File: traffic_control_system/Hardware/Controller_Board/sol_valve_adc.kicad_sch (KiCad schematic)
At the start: 45 parts, among them U21 TL084, U22 TL081, U23 APX321SEG

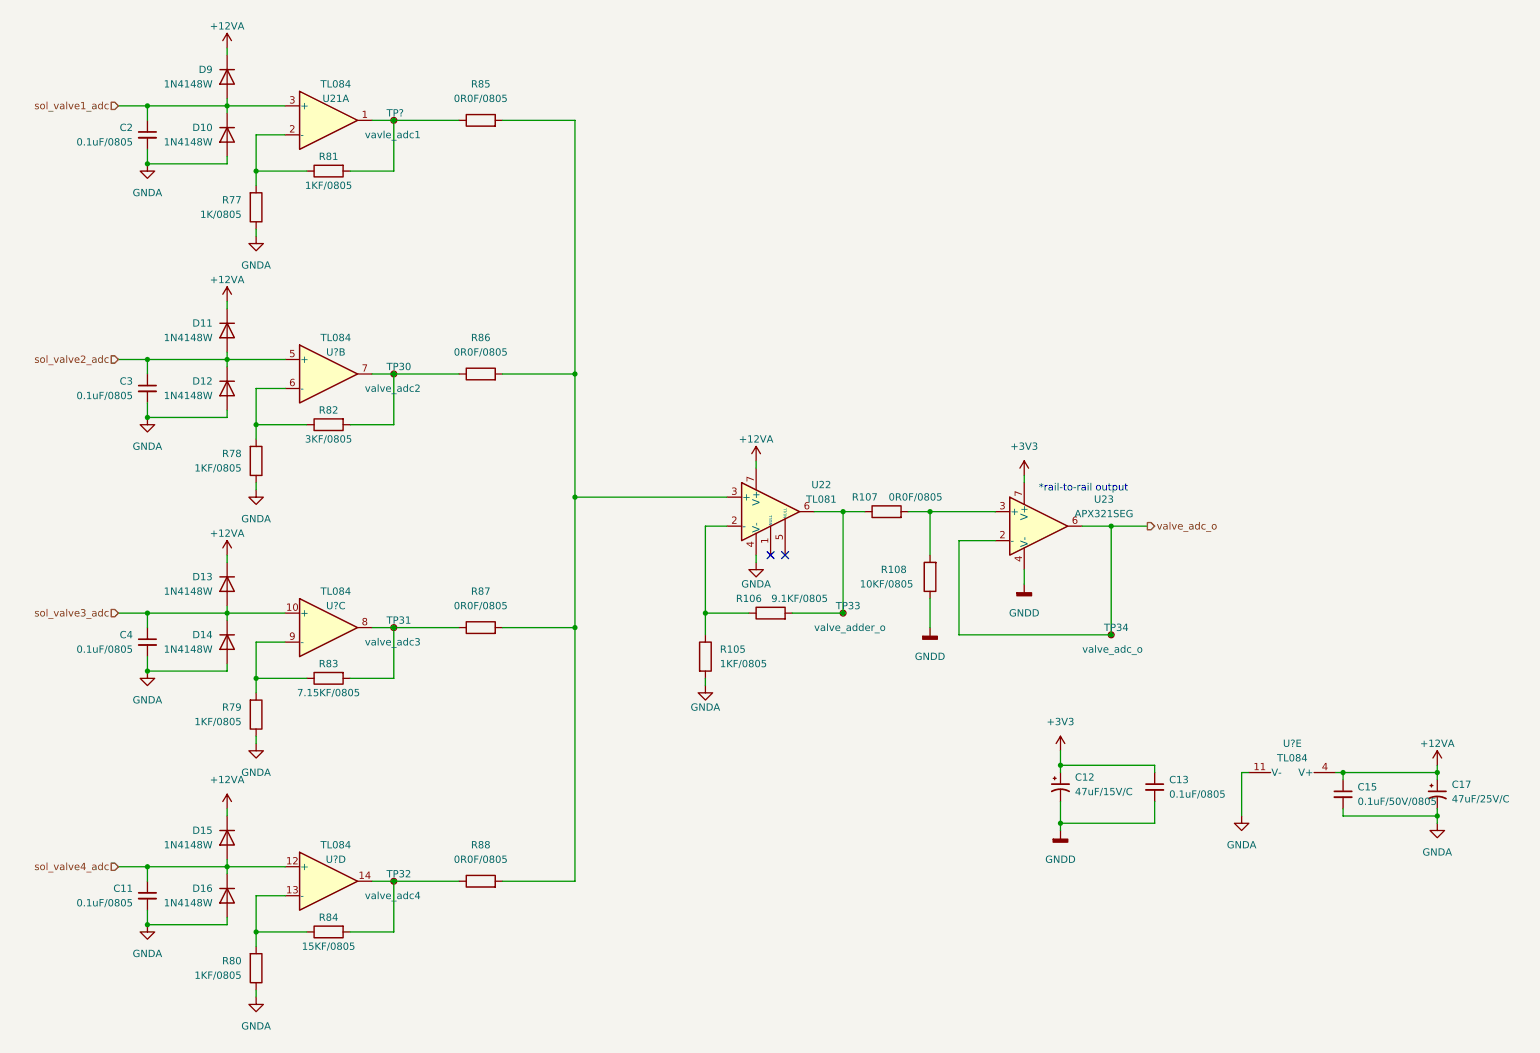
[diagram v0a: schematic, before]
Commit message: issue : 깃 커밋 히스토리 정리를 위한 원본 저장소의 브랜치 분리 작업[TRAFFIC-CONTROL6]
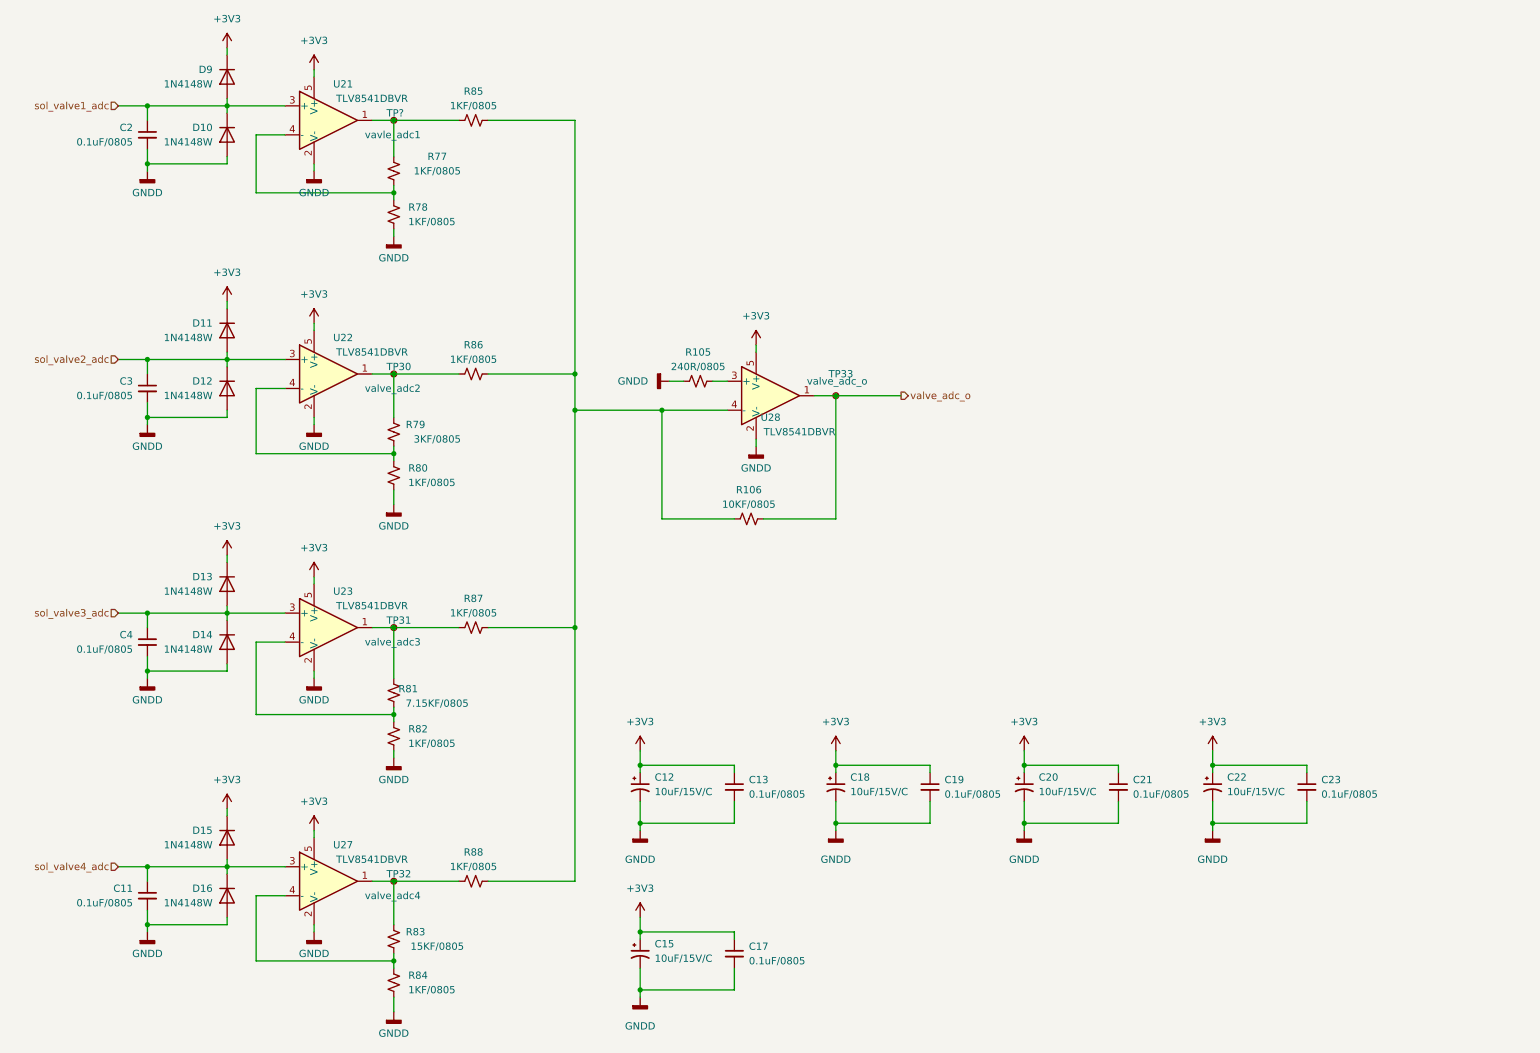
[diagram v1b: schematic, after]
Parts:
- removed C15: 0.1uF/50V/0805, symbol Device:C_Small
- removed C17: 47uF/25V/C, symbol Device:C_Polarized_Small_US
- removed R105, R77, R78, R79, R80, R81: 1KF/0805, symbol Device:R
- removed R106: 9.1KF/0805, symbol Device:R
- removed R107, R86, R87, R88: 0R0F/0805, symbol Device:R
- removed R108: 10KF/0805, symbol Device:R
- removed R82: 3KF/0805, symbol Device:R
- removed R83: 7.15KF/0805, symbol Device:R
- removed R84: 15KF/0805, symbol Device:R
- removed R85: R, symbol Device:R
- removed TP34: valve_adc_o, symbol Connector:TestPoint_Small
- removed U21, U? (x4): TL084, symbol Amplifier_Operational:TL084
- removed U22: TL081, symbol Amplifier_Operational:TL081
- removed U23: APX321SEG, Package_SO:SOIC-8_3.9x4.9mm_P1.27mm, symbol Amplifier_Operational:OPA196xD
- added C15, C18, C20, C22: 10uF/15V/C, symbol Device:C_Polarized_Small_US
- added C17, C19, C21, C23: 0.1uF/0805, symbol Device:C_Small
- added R105: 240R/0805, symbol Device:R_Small_US
- added R106: 10KF/0805, symbol Device:R_Small_US
- added R77, R78, R80, R82, R84, R85, R86, R87, R88: 1KF/0805, symbol Device:R_Small_US
- added R79: 3KF/0805, symbol Device:R_Small_US
- added R81: 7.15KF/0805, symbol Device:R_Small_US
- added R83: 15KF/0805, symbol Device:R_Small_US
- added U21, U22, U23, U27, U28: TLV8541DBVR, Package_TO_SOT_SMD:SOT-23-5, symbol Amplifier_Operational:TLV2371DBV
- C12: value 47uF/15V/C -> 10uF/15V/C
- TP33: value valve_adder_o -> valve_adc_o
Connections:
- net +12VA is gone; now on net +3V3: D11.1 (K), D13.1 (K), D15.1 (K), D9.1 (K)
- net GNDA is gone; now on net GNDD: C11.2, C2.2, C3.2, C4.2, D10.2 (A), D12.2 (A), D14.2 (A), D16.2 (A)
- net +3V3: now also C15.1, C17.1, C18.1, C19.1, C20.1, C21.1, C22.1, C23.1, U21.5 (V+), U22.5 (V+), U23.5 (V+), U27.5 (V+), U28.5 (V+)
- net GNDD: now also C15.2, C17.2, C18.2, C19.2, C20.2, C21.2, C22.2, C23.2, R105.2, R78.1, R80.1, R82.1, R84.1, U21.2 (V-), U22.2 (V-), U23.2 (V-), U27.2 (V-), U28.2 (V-)
- net sol_valve1_adc: now also U21.3 (+)
- net sol_valve2_adc: now also U22.3 (+)
- net sol_valve3_adc: now also U23.3 (+)
- net sol_valve4_adc: now also U27.3 (+)
- net valve_adc_o: now also TP33.1, R106.2, U28.1
- net at TP32.1: now also R83.1, R88.2, U27.1
- net at TP31.1: now also R81.1, R87.2, U23.1
- net at TP?.1: now also R77.1, R85.2, U21.1
- net at TP30.1: now also R79.1, R86.2, U22.1
- new net: R81.2, R82.2, U23.4 (-)
- new net: R106.1, R85.1, R86.1, R87.1, R88.1, U28.4 (-)
- new net: R79.2, R80.2, U22.4 (-)
- new net: R105.1, U28.3 (+)
- new net: R77.2, R78.2, U21.4 (-)
- new net: R83.2, R84.2, U27.4 (-)
- no-connect marks 2 -> 0
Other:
- note removed: "*rail-to-rail output"
- moved on the sheet: C12, C13
